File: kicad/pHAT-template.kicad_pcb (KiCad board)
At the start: 2 copper layers, 65 x 30 mm, 5 parts

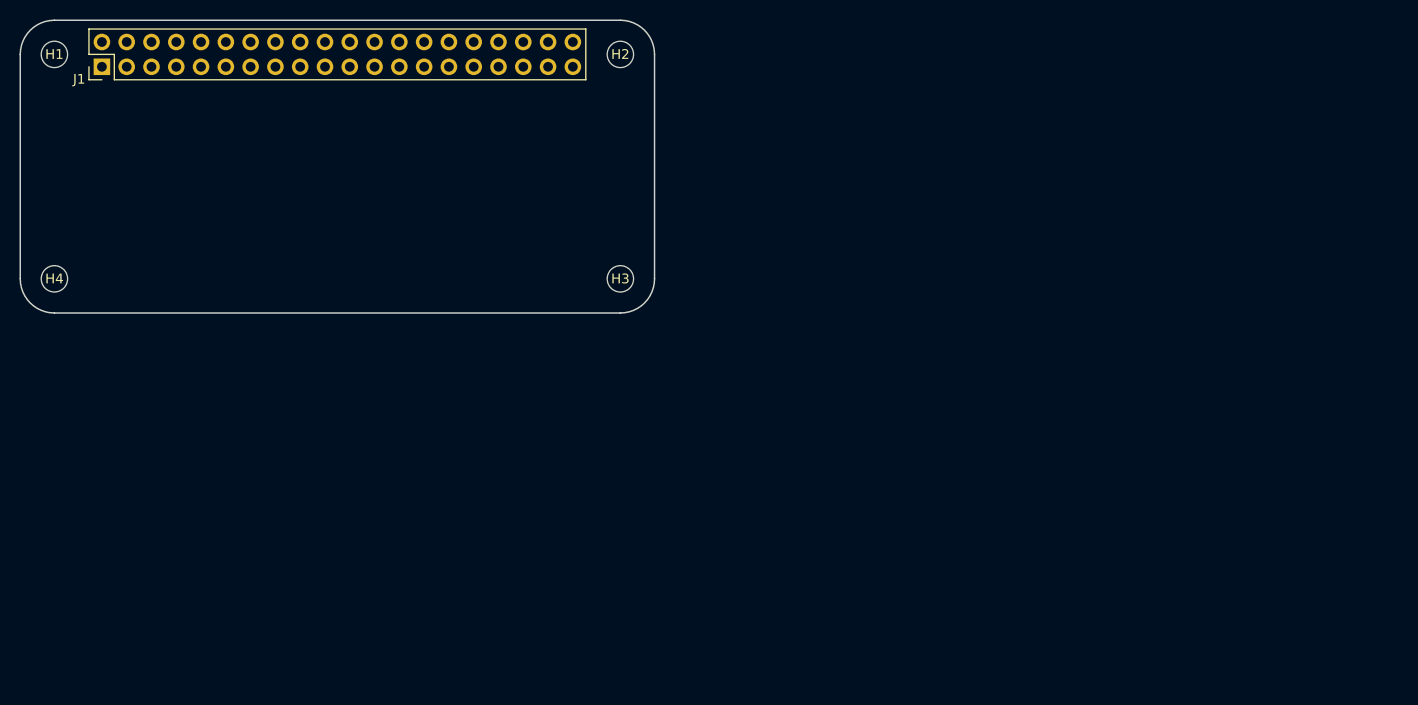
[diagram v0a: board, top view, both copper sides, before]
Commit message: moved pcb onto sheet
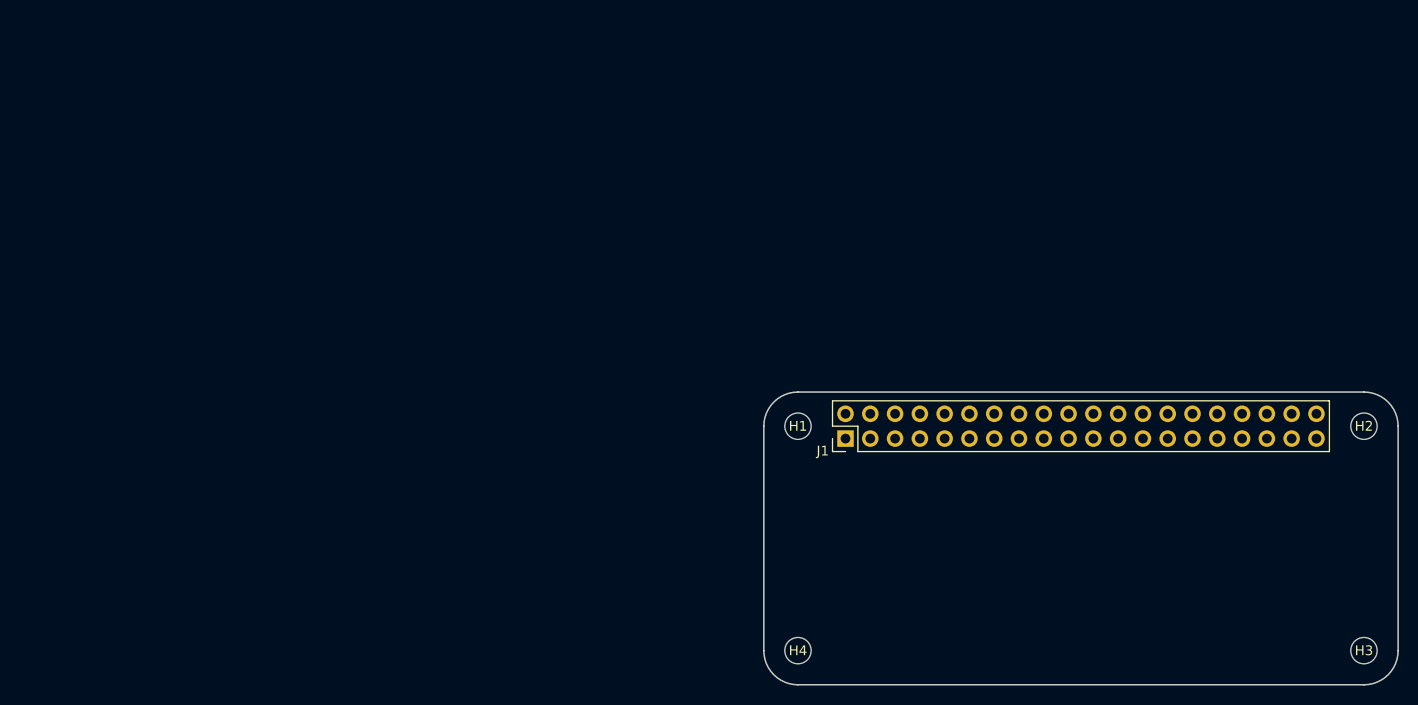
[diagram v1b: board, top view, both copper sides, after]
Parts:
- moved H1 85.2 mm to (47.2, 38.1)
- moved H2 85.2 mm to (105.2, 38.1)
- moved H3 85.2 mm to (105.2, 61.1)
- moved H4 85.2 mm to (47.2, 61.1)
- moved J1 85.2 mm to (52.1, 39.4)
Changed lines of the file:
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@@
     (links 9)
     (no_connects 9)
-    (area 141.118718 100.3286 158.423482 156.6686)
+    (area -32.575001 -3.575001 32.575001 27.775)
     (thickness 1.6)
     (drawings 8)
@@
   )
   (module Mounting_Holes:MountingHole_2.7mm_M2.5 (layer F.Cu)
-    (at -29 0)
+    (at 47.2 38.1)
     (descr "Mounting Hole 2.7mm, no annular, M2.5")
     (tags "mounting hole 2.7mm no annular m2.5")
@@
   )
   (module Mounting_Holes:MountingHole_2.7mm_M2.5 (layer F.Cu)
-    (at 29 0)
+    (at 105.2 38.1)
     (descr "Mounting Hole 2.7mm, no annular, M2.5")
     (tags "mounting hole 2.7mm no annular m2.5")
@@
   )
   (module Mounting_Holes:MountingHole_2.7mm_M2.5 (layer F.Cu)
-    (at 29 23)
+    (at 105.2 61.1)
     (descr "Mounting Hole 2.7mm, no annular, M2.5")
     (tags "mounting hole 2.7mm no annular m2.5")
@@
   )
   (module Mounting_Holes:MountingHole_2.7mm_M2.5 (layer F.Cu)
-    (at -29 23)
+    (at 47.2 61.1)
     (descr "Mounting Hole 2.7mm, no annular, M2.5")
     (tags "mounting hole 2.7mm no annular m2.5")
@@
   )
   (module Pin_Headers:Pin_Header_Straight_2x20_Pitch2.54mm (layer F.Cu)
-    (at -24.13 1.27 90)
+    (at 52.07 39.37 90)
     (descr "Through hole straight pin header, 2x20, 2.54mm pitch, double rows")
     (tags "Through hole pin header THT 2x20 2.54mm double row")
@@
     )
   )
-  (gr_arc (start 29 0) (end 29 -3.5) (angle 90) (layer Edge.Cuts) (width 0.15))
-  (gr_arc (start 29 23) (end 32.5 23) (angle 90) (layer Edge.Cuts) (width 0.15))
-  (gr_arc (start -29 23) (end -29 26.5) (angle 90) (layer Edge.Cuts) (width 0.15))
-  (gr_arc (start -29 0) (end -32.5 0) (angle 90) (layer Edge.Cuts) (width 0.15))
-  (gr_line (start 32.5 0) (end 32.5 23) (layer Edge.Cuts) (width 0.15))
-  (gr_line (start -32.5 0) (end -32.5 23) (layer Edge.Cuts) (width 0.15))
-  (gr_line (start -29 26.5) (end 29 26.5) (layer Edge.Cuts) (width 0.15))
-  (gr_line (start -29 -3.5) (end 29 -3.5) (layer Edge.Cuts) (width 0.15))
+  (gr_arc (start 105.2 38.1) (end 105.2 34.6) (angle 90) (layer Edge.Cuts) (width 0.15))
+  (gr_arc (start 105.2 61.1) (end 108.7 61.1) (angle 90) (layer Edge.Cuts) (width 0.15))
+  (gr_arc (start 47.2 61.1) (end 47.2 64.6) (angle 90) (layer Edge.Cuts) (width 0.15))
+  (gr_arc (start 47.2 38.1) (end 43.7 38.1) (angle 90) (layer Edge.Cuts) (width 0.15))
+  (gr_line (start 108.7 38.1) (end 108.7 61.1) (layer Edge.Cuts) (width 0.15))
+  (gr_line (start 43.7 38.1) (end 43.7 61.1) (layer Edge.Cuts) (width 0.15))
+  (gr_line (start 47.2 64.6) (end 105.2 64.6) (layer Edge.Cuts) (width 0.15))
+  (gr_line (start 47.2 34.6) (end 105.2 34.6) (layer Edge.Cuts) (width 0.15))
 )
